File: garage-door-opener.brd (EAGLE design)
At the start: 72.1 x 43.2 mm, 19 parts, among them IC1 317T, K1 RR1A, T1 BC547, X1 Connector

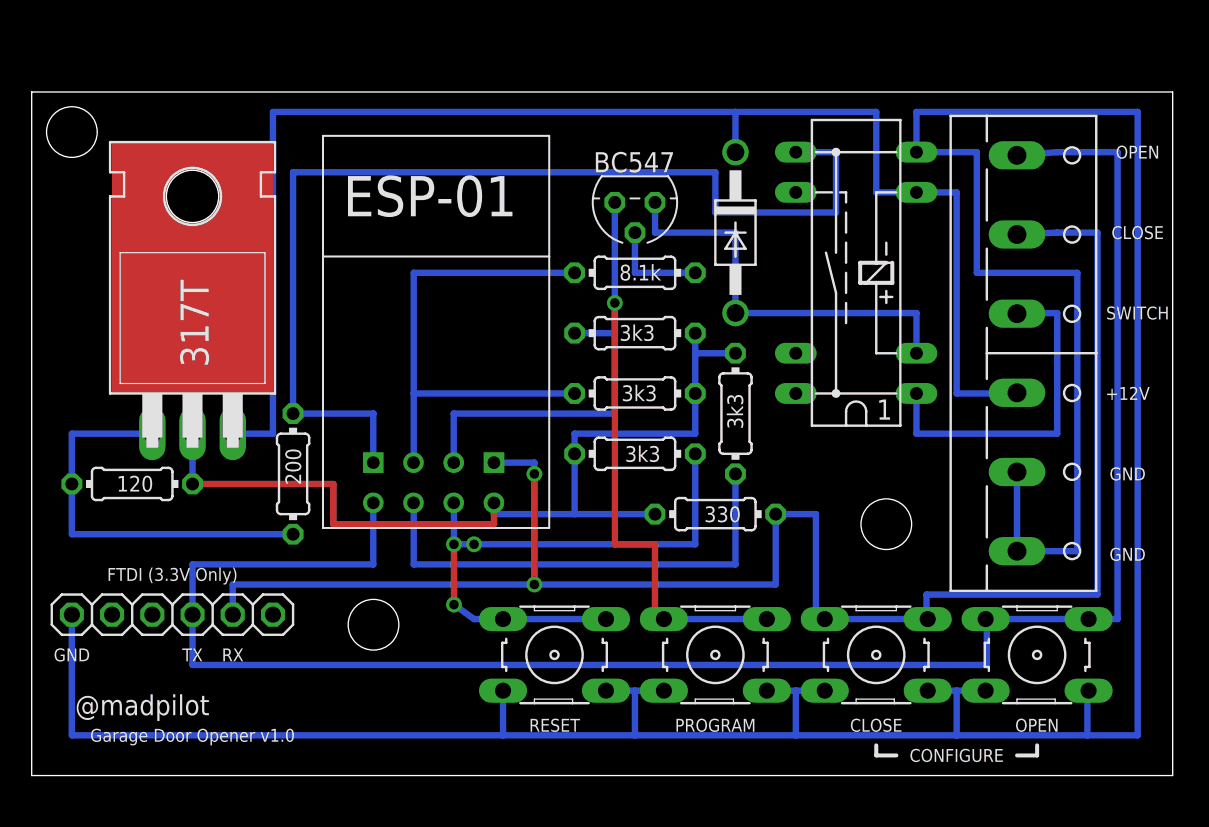
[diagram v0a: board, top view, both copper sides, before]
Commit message: Rerouting board to use switch mode PSU, and removing development switches and pads. Need to use the pogoable version of the ESP12
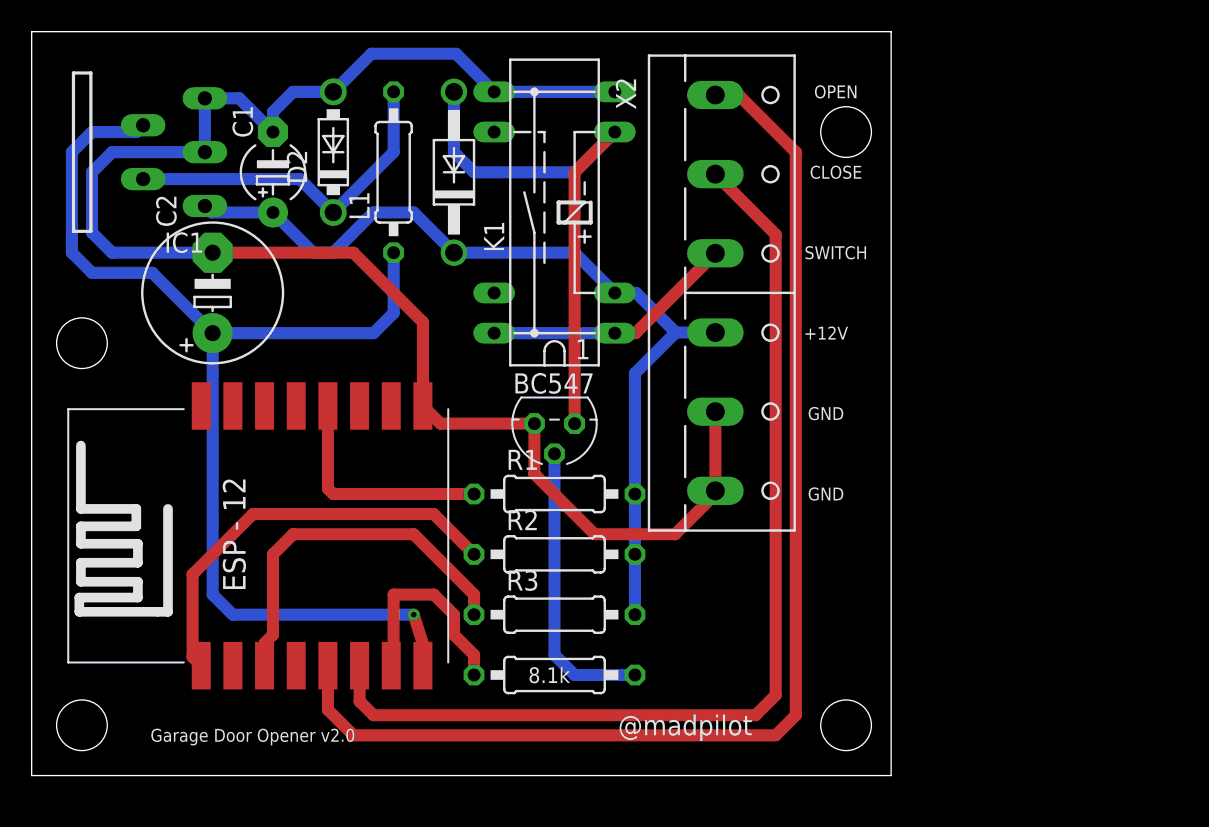
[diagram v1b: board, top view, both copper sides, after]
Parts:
- removed JP1: FTDI (3.3V only), adafruit:1X06
- removed R4: 3k3, resistor:0204/7
- removed R5: 330, resistor:0204/7
- removed R6: 200, resistor:0204/7
- removed R7: 120, resistor:0204/7
- removed S1: Close, switch-omron:B3F-10XX
- removed S2: Program, switch-omron:B3F-10XX
- removed S3: Open, switch-omron:B3F-10XX
- removed S4: Reset, switch-omron:B3F-10XX
- removed U$1: ESP01, esp8266modules:ESP01
- removed X1: Connector, con-wago-500:W237-6
- added C1: 47uF, rcl:E5-4
- added C2: 220uF, rcl:E5-8,5
- added D2: 1N5819-T, diode:DO41-7.6
- added L1: 220uH, eagle-ltspice:0207/10
- added U1: (no value), esp8266modules:ESP12-SMD
- added X2: Connector, con-wago-500:W237-6
- IC1: value 317T -> LM2575-3.3T; device linear:TO220H -> lm2575:TO220-5
- R1, R2, R3, R8: device resistor:0204/7 -> resistor:0207/10
- moved R8 25.9 mm to (33.0, 43.2), turned to 180 degrees
- moved K1 19.4 mm to (33.0, 72.4)
- moved D1 18.2 mm to (26.7, 74.9), turned to 90 degrees
- moved R3 17.1 mm to (33.0, 47.0), turned to 0 degrees
- moved T1 14.9 mm to (33.0, 59.1)
- moved R2 11.4 mm to (33.0, 50.8)
- moved R1 11.4 mm to (33.0, 54.6)
- moved IC1 10.8 mm to (2.54, 76.2), turned to 90 degrees
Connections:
- removed net 3.3V: IC1.2, R1.2, R2.2, R3.2, R4.2, R5.2, R7.2, U$1.VCC
- removed net RX: JP1.5, R5.1, S1.1, S1.2, U$1.RX, X1.2
- removed net TX: JP1.4, S3.1, S3.2, U$1.TX, X1.1
- new net N$11: U1.GPIO14, X2.1
- new net N$4: C2.+, IC1.4, L1.1, U1.VCC
- new net N$9: R8.2, U1.GPIO13
- net GND: now also C1.-, C2.-, D2.A, IC1.3, IC1.5, T1.1, U1.GND, X2.5, X2.6; no longer JP1.1, R6.1, S1.3, S1.4, S2.3, S2.4, S3.3, S3.4, S4.3, S4.4, U$1.GND, X1.5, X1.6
- net N$1: now also K1.6; no longer K1.2
- net N$10: now also U1.GPIO12, X2.2; no longer K1.1, K1.14, X1.3
- net N$2: now also R8.1; no longer R8.2
- net N$3: now also D2.C, IC1.2, L1.2; no longer IC1.1, R6.2, R7.1
- net N$5: now also K1.1, K1.14, X2.3; no longer R1.1, S2.1, S2.2, T1.1, U$1.GPIO0
- net N$6: now also R3.1, U1.CH_PD; no longer R2.1, R8.1, U$1.GPIO2
- net N$7: now also R1.1, U1.GPIO0; no longer R3.1, U$1.CH_PD
- net N$8: now also R2.1, U1.RESET; no longer R4.1, S4.1, S4.2, U$1.RST
- net VCC: now also C1.+, IC1.1, K1.2, R1.2, R2.2, R3.2, X2.4; no longer IC1.3, K1.6, X1.4
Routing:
- net GND: track 266.7 -> 103.9 mm
- net TX: track 118.9 -> 0.00 mm
- net RX: track 107.5 -> 0.00 mm, vias 2 -> 0
- net N$11: track 0.00 -> 75.7 mm
- net N$4: track 0.00 -> 71.4 mm, vias 0 -> 1
- net 3.3V: track 58.6 -> 0.00 mm
- net N$5: track 58.7 -> 16.1 mm, vias 1 -> 0
- net N$10: track 21.6 -> 63.9 mm
- net VCC: track 90.2 -> 56.5 mm
- net N$7: track 29.9 -> 14.6 mm
- net N$9: track 0.00 -> 13.2 mm
- net N$2: track 6.35 -> 18.3 mm
- net N$8: track 37.3 -> 26.4 mm, vias 3 -> 0
- net N$6: track 32.3 -> 23.3 mm
- net N$1: track 26.0 -> 35.0 mm
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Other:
- board size 72.1 x 43.2 mm -> 54.3 x 47 mm
- board text added: "Garage Door Opener v2.0"
- board text removed: "CONFIGURE"
- board text removed: "FTDI (3.3V Only)"
- board text removed: "Garage Door Opener v1.0"
- board text removed: "PROGRAM"
- board text removed: "RESET"
- board text removed: "RX"
- board text removed: "TX"

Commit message: Adding pull up resistors for all inputs for boot, hardwiring CH_PD, adding a config button to turn on the config website
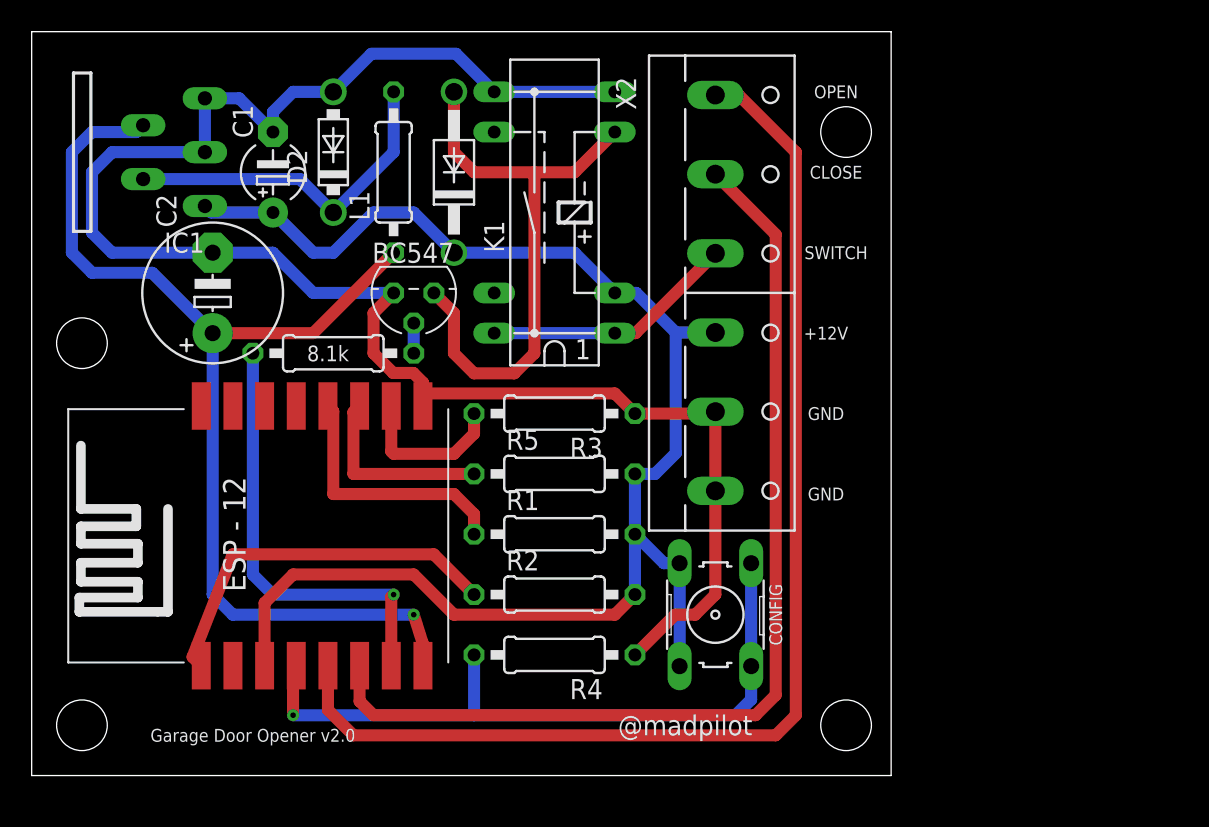
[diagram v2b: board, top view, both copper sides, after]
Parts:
- added R4, R5: 3k3, resistor:0207/10
- added S1: (no value), switch-omron:B3F-10XX
- moved R8 24.7 mm to (19.1, 63.5)
- moved R3 12.7 mm to (33.0, 59.7), turned to 180 degrees
- moved T1 12.1 mm to (24.1, 67.3)
- moved R1 2.54 mm to (33.0, 52.1)
- moved R2 2.54 mm to (33.0, 48.3)
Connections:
- new net N$12: R4.2, S1.3, S1.4, U1.GPIO16
- new net N$13: R5.1, U1.GPIO2
- net GND: now also R3.1, R4.1
- net N$6: now also R3.2, U1.GPIO15; no longer R3.1, U1.CH_PD
- net VCC: now also R5.2, S1.1, S1.2, U1.CH_PD; no longer R3.2
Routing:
- net N$12: track 0.00 -> 45.0 mm, vias 0 -> 1
- net VCC: track 56.5 -> 95.8 mm
- net N$2: track 18.3 -> 1.91 mm
- net N$9: track 13.2 -> 27.9 mm, vias 0 -> 1
- net N$6: track 23.3 -> 9.96 mm
- net N$13: track 0.00 -> 12.1 mm
- net GND: track 103.9 -> 113.0 mm
- net N$1: track 35.0 -> 37.4 mm
- net N$8: track 26.4 -> 24.0 mm
- net N$4: track 71.4 -> 69.1 mm
- net N$7: track 14.6 -> 16.4 mm
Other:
- board text added: "CONFIG"

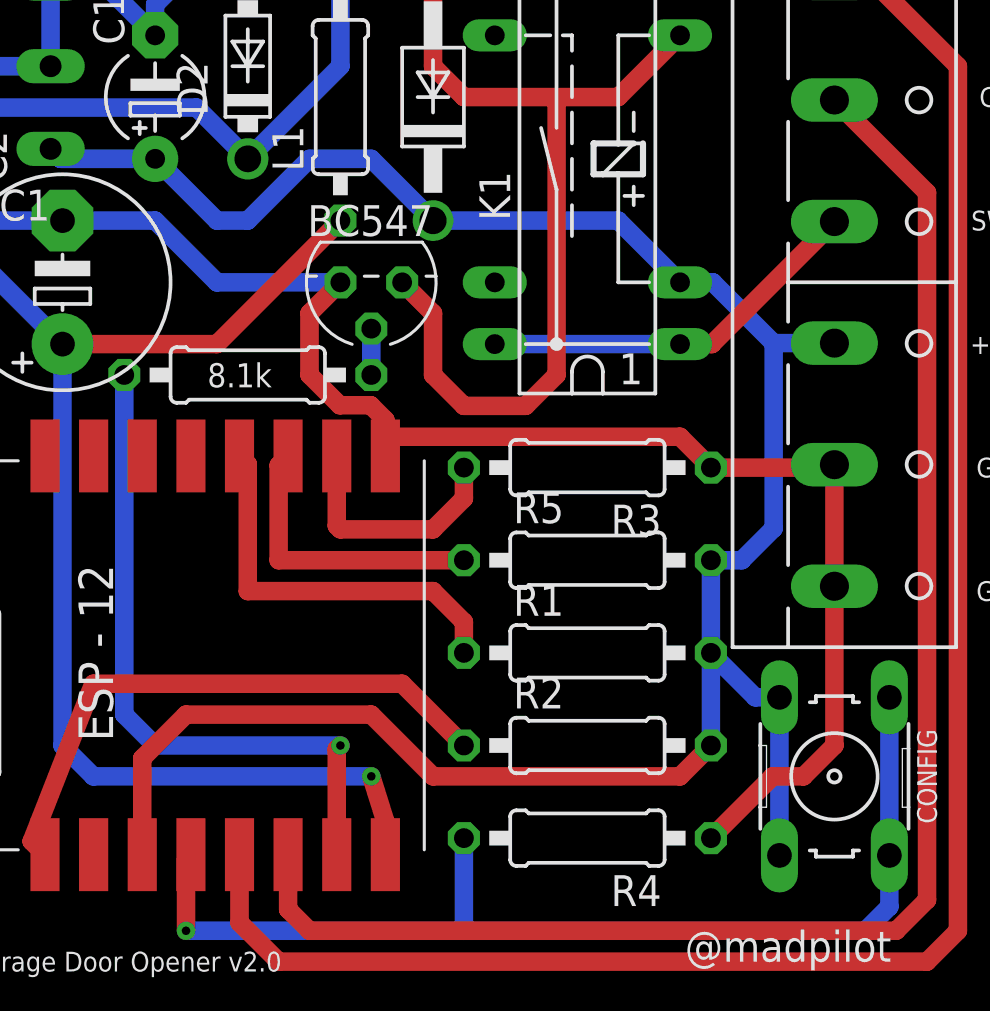
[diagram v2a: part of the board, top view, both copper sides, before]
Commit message: Fixing missing node on the VCC net, 12V in was incorrectly linked to VCC. Moved to VIN
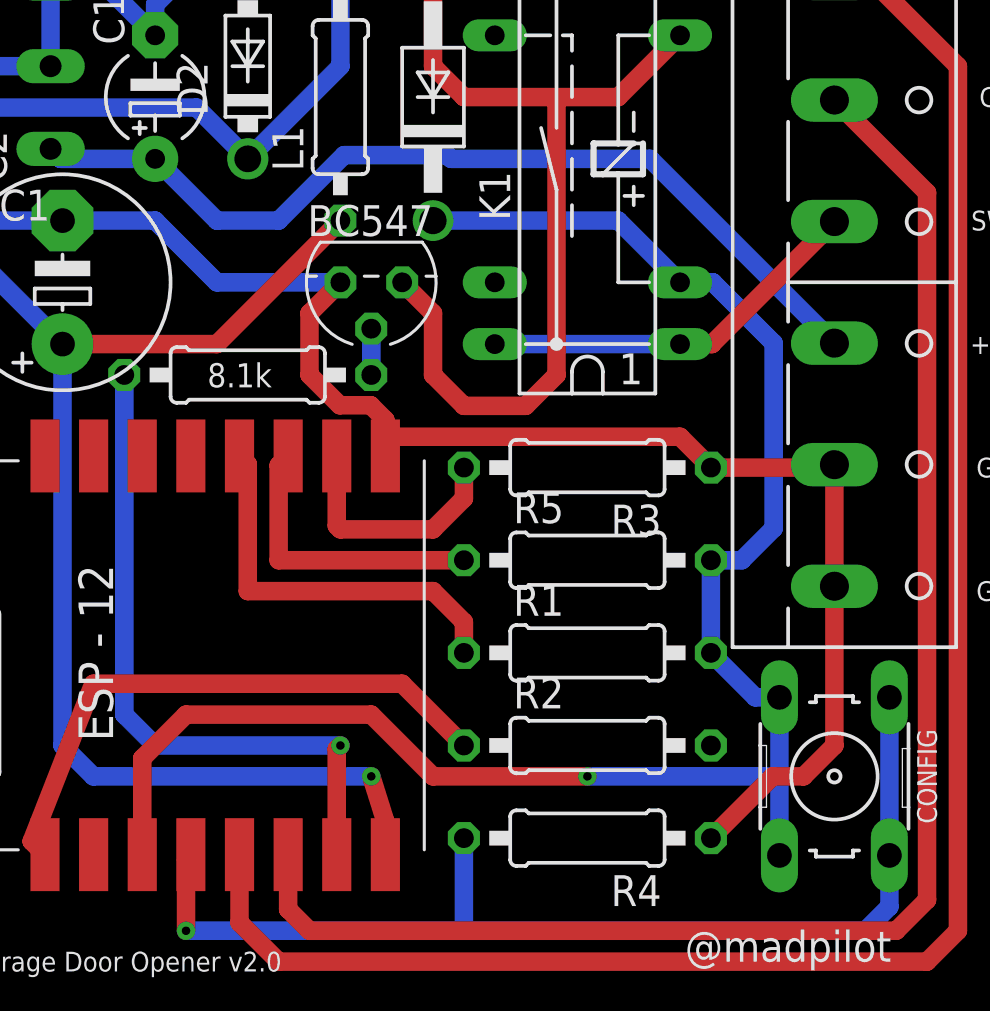
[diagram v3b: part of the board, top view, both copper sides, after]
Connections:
- new net VIN: C1.+, IC1.1, X2.4
- net VCC: no longer C1.+, IC1.1, X2.4
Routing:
- net VIN: track 0.00 -> 37.8 mm
- net VCC: track 95.8 -> 72.7 mm, vias 0 -> 1
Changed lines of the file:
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@@
 <drawing>
 <settings>
-<setting alwaysvectorfont="no"/>
+<setting alwaysvectorfont="yes"/>
 <setting keepoldvectorfont="yes"/>
 <setting verticaltext="up"/>
@@
 <signal name="VCC">
 <contactref element="D1" pad="C"/>
-<contactref element="IC1" pad="1"/>
-<contactref element="C1" pad="+"/>
-<contactref element="R2" pad="2"/>
 <contactref element="R1" pad="2"/>
 <contactref element="K1" pad="2"/>
-<contactref element="X2" pad="4"/>
-<wire x1="10.94" y1="72.8" x2="11.35" y2="72.39" width="0.762" layer="16"/>
-<wire x1="11.35" y1="72.39" x2="15.24" y2="72.39" width="0.762" layer="16"/>
-<wire x1="26.67" y1="69.85" x2="24.13" y2="72.39" width="0.762" layer="16"/>
-<wire x1="24.13" y1="72.39" x2="21.59" y2="72.39" width="0.762" layer="16"/>
-<wire x1="21.59" y1="72.39" x2="19.05" y2="69.85" width="0.762" layer="16"/>
-<wire x1="19.05" y1="69.85" x2="17.78" y2="69.85" width="0.762" layer="16"/>
-<wire x1="17.78" y1="69.85" x2="15.24" y2="72.39" width="0.762" layer="16"/>
 <wire x1="26.67" y1="69.85" x2="34.29" y2="69.85" width="0.762" layer="16"/>
 <wire x1="34.29" y1="69.85" x2="36.83" y2="67.31" width="0.762" layer="16"/>
-<wire x1="40.68" y1="64.81" x2="43.18" y2="64.81" width="0.762" layer="16"/>
 <wire x1="36.83" y1="67.31" x2="38.18" y2="67.31" width="0.762" layer="16"/>
 <wire x1="38.18" y1="67.31" x2="40.68" y2="64.81" width="0.762" layer="16"/>
 <contactref element="S1" pad="1"/>
 <contactref element="S1" pad="2"/>
-<wire x1="40.9194" y1="50.2412" x2="40.9194" y2="43.7388" width="0.762" layer="16"/>
+<wire x1="40.9194" y1="50.2412" x2="40.9194" y2="46.99" width="0.762" layer="16"/>
 <contactref element="U1" pad="CH_PD"/>
 <contactref element="R5" pad="2"/>
+<wire x1="40.9194" y1="46.99" x2="40.9194" y2="43.7388" width="0.762" layer="16"/>
 <wire x1="38.1" y1="55.88" x2="38.1" y2="52.07" width="0.762" layer="16"/>
 <wire x1="38.1" y1="52.07" x2="39.9288" y2="50.2412" width="0.762" layer="16"/>
@@
 <wire x1="40.68" y1="57.19" x2="40.68" y2="64.81" width="0.762" layer="16"/>
 <wire x1="39.37" y1="55.88" x2="40.68" y2="57.19" width="0.762" layer="16"/>
-<wire x1="38.1" y1="48.26" x2="38.1" y2="52.07" width="0.762" layer="16"/>
-<wire x1="38.1" y1="48.26" x2="36.83" y2="46.99" width="0.762" layer="1"/>
-<wire x1="36.83" y1="46.99" x2="26.67" y2="46.99" width="0.762" layer="1"/>
-<wire x1="26.67" y1="46.99" x2="24.13" y2="49.53" width="0.762" layer="1"/>
+<wire x1="24.13" y1="49.53" x2="26.67" y2="46.99" width="0.762" layer="1"/>
 <wire x1="24.13" y1="49.53" x2="16.51" y2="49.53" width="0.762" layer="1"/>
 <wire x1="16.51" y1="49.53" x2="14.71" y2="47.73" width="0.762" layer="1"/>
 <wire x1="14.71" y1="47.73" x2="14.71" y2="43.77" width="0.762" layer="1"/>
+<contactref element="R2" pad="2"/>
+<wire x1="26.67" y1="46.99" x2="33.02" y2="46.99" width="0.762" layer="1"/>
+<via x="33.02" y="46.99" extent="1-16" drill="0.35"/>
+<wire x1="33.02" y1="46.99" x2="40.9194" y2="46.99" width="0.762" layer="16"/>
+<wire x1="39.9288" y1="50.2412" x2="38.1" y2="48.26" width="0" layer="19" extent="16-16"/>
 </signal>
 <signal name="N$4">
@@
 <wire x1="20.32" y1="55.88" x2="20.32" y2="59.78" width="0.762" layer="1"/>
 </signal>
+<signal name="VIN">
+<contactref element="IC1" pad="1"/>
+<contactref element="C1" pad="+"/>
+<wire x1="10.94" y1="72.8" x2="11.35" y2="72.39" width="0.762" layer="16"/>
+<wire x1="11.35" y1="72.39" x2="15.24" y2="72.39" width="0.762" layer="16"/>
+<contactref element="X2" pad="4"/>
+<wire x1="15.24" y1="72.39" x2="17.78" y2="69.85" width="0.762" layer="16"/>
+<wire x1="17.78" y1="69.85" x2="20.32" y2="69.85" width="0.762" layer="16"/>
+<wire x1="27.25918125" y1="72.5424" x2="27.41158125" y2="72.39" width="0.762" layer="16"/>
+<wire x1="20.32" y1="69.85" x2="23.0124" y2="72.5424" width="0.762" layer="16"/>
+<wire x1="23.0124" y1="72.5424" x2="27.25918125" y2="72.5424" width="0.762" layer="16"/>
+<wire x1="35.6" y1="72.39" x2="43.18" y2="64.81" width="0.762" layer="16"/>
+<wire x1="27.41158125" y1="72.39" x2="35.6" y2="72.39" width="0.762" layer="16"/>
+</signal>
 </signals>
